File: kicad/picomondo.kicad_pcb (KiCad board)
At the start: 4 copper layers, 120 x 90 mm, 289 parts, among them J1 EdgeLock J1, J10 SWD, J11 Barrel 5.5x2.1, J12 Terminal 2P, J13 USB-C, J14 Arduino power, J15 Arduino analog, J16 Arduino digital 0-7, J17 Arduino digital 8-13, J18 Pico left (pins 1-20), J19 Pico right (pins 40-21), J2 EdgeLock J2, J3 EdgeLock J3, J4 EdgeLock J4, J5 EdgeLock J5, J6 EdgeLock J6, J7 J7 5V out, J8 J8 V_INPUT out, J9 EdgeLock J9, Q1 CSD18543Q3A, Q2 CSD18543Q3A, Q3 SI2305A, Q4 MMBT3904, Q5 DMP4015SSS-13, Q6 MMBT3904, Q7 SI2305A, Q8 MMBT3904, SW1 BOOTSEL, SW2 RESET, U1 RP2350B, U10 STUSB4500, U11 microSD, U2 W25Q128JVS, U3 DNP second memory, U4 TPS55288, U5 AP2112K-3.3, U6 AP2112K-3.3, U7 INA226 (0x40), U8 INA226 (0x41), U9 USBLC6-2SC6, Y1 ABM8-272-T3

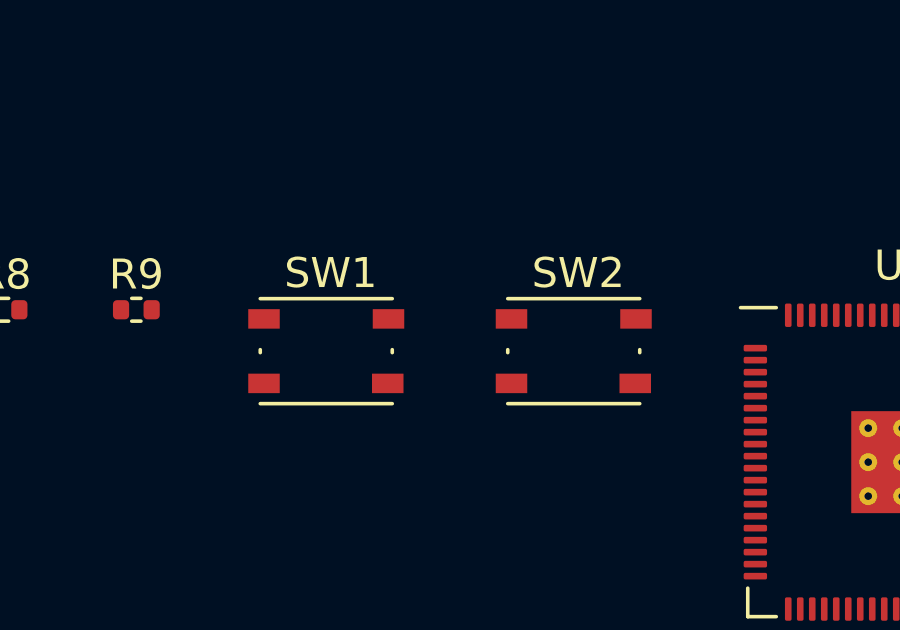
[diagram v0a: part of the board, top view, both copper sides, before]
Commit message: Pick JLCPCB parts for the whole BOM and add BOM/CPL generation
Adds bom/parts.csv (LCSC numbers and MPNs), scripts to apply it to the schematic and
board and to generate the JLCPCB BOM, CPL and a live stock report. Swaps the
BOOTSEL/RESET switch to a basic 5.1 mm part with a matching footprint, and replaces
out-of-stock parts (SS54, WS2812B, 10u caps, SWD header).

Co-Authored-By: Claude Sonnet 5.5 <noreply@anthropic.com>
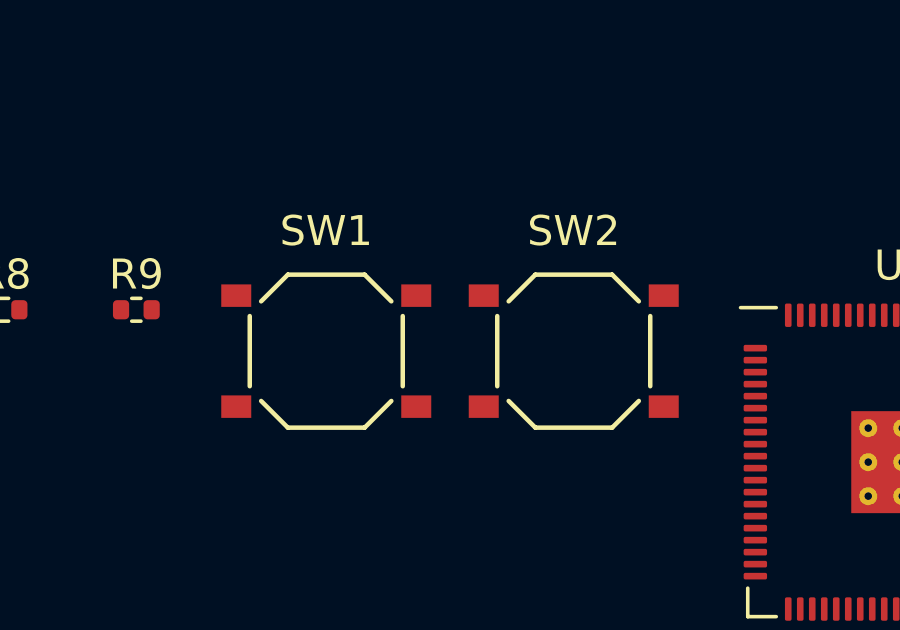
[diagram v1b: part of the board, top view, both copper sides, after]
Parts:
- SW1, SW2: footprint Button_Switch_SMD:SW_Push_1P1T_NO_Vertical_Wuerth_434133025816 -> picomondo:SW_SMD_TS-1187A_5.1x5.1

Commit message: Rework board layout, swap SWD header to through-hole, add Qwiic port
- SWD (J10) is now a 1x3 2.54 mm through-hole pin header footprint
  (SWCLK, GND, SWDIO) instead of the JST SH connector; removed from the
  JLCPCB BOM.
- Add J20 Qwiic connector (XY-SM04B-SRSS-TB) on the I2C bus: GND, +3V3,
  GPIO20 (SDA), GPIO21 (SCL), mounting tabs to GND.
- Placement/routing progress and the helper scripts used for it.

DRC still reports open items (unrouted RUN/GPIO24/GPIO29/QSPI_SD0 nets,
R108/GPIO23 and NT1/GPIO20 shorts, J12 edge clearance, silkscreen
overlaps); to be fixed in follow-up commits.

Co-Authored-By: Claude Sonnet 5.5 <noreply@anthropic.com>
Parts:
- removed JP1, JP2, JP3, JP4, JP5, JP6, JP7, JP8: LED enable, Jumper:SolderJumper-2_P1.3mm_Open_RoundedPad1.0x1.5mm
- added CN1: QWICC, JLCImport:XY-SM04B-SRSS-TB, F.Cu at (146.3, 80.1)
- J10: footprint Connector_JST:JST_SH_SM03B-SRSS-TB_1x03-1MP_P1.00mm_Horizontal -> Connector_PinHeader_2.54mm:PinHeader_1x03_P2.54mm_Horizontal
- TP1, TP10, TP11, TP12, TP13, TP14, TP15, TP16, TP17, TP2, TP3, TP4, TP5, TP6, TP7, TP8, TP9: moved to B.Cu
- moved R95 446.6 mm to (41.1, 43.0), turned to -90 degrees
- moved R97 429.0 mm to (67.7, 43.0), turned to -90 degrees
- moved R94 427.1 mm to (56.4, 43.0), turned to -90 degrees
- moved R99 411.5 mm to (94.3, 43.0), turned to -90 degrees
- moved R96 409.7 mm to (83.0, 43.0), turned to -90 degrees
- moved R89 409.0 mm to (46.0, 107.0), turned to 90 degrees
- moved R88 406.5 mm to (44.0, 107.0), turned to 90 degrees
- moved R91 406.5 mm to (57.3, 107.0), turned to 90 degrees
- moved R90 404.1 mm to (55.3, 107.0), turned to 90 degrees
- moved R98 392.2 mm to (109.6, 43.0), turned to -90 degrees
- moved R93 384.9 mm to (87.9, 103.2), turned to 90 degrees
- moved R92 378.0 mm to (90.4, 103.1), turned to 90 degrees
- moved R86 369.1 mm to (72.6, 107.0), turned to 90 degrees
- moved R87 364.3 mm to (81.9, 107.0), turned to 90 degrees
- moved R73 349.4 mm to (43.1, 43.0), turned to -90 degrees
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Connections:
- R100 pad 1: /GPIO indicators/LED46_J -> GPIO46
- R101 pad 1: /GPIO indicators/LED47_J -> GPIO47
- R108 pad 2: GPIO23 -> unconnected-(R108-Pad2)
- R94 pad 1: /GPIO indicators/LED40_J -> GPIO40
- R95 pad 1: /GPIO indicators/LED41_J -> GPIO41
- R96 pad 1: /GPIO indicators/LED42_J -> GPIO42
- R97 pad 1: /GPIO indicators/LED43_J -> GPIO43
- R98 pad 1: /GPIO indicators/LED44_J -> GPIO44
- R99 pad 1: /GPIO indicators/LED45_J -> GPIO45
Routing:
- net +3V3: track 0.00 -> 471.4 mm, vias 0 -> 72
- net GND: track 0.00 -> 377.3 mm, vias 0 -> 110
- net +5V: track 0.00 -> 291.2 mm, vias 0 -> 21
- net GPIO20: track 0.00 -> 240.9 mm, vias 0 -> 24
- net V_INPUT: track 0.00 -> 230.0 mm, vias 0 -> 23
- net GPIO21: track 0.00 -> 221.7 mm, vias 0 -> 20
- net +3V3_AUX: track 0.00 -> 145.1 mm, vias 0 -> 9
- net VBUS: track 0.00 -> 128.5 mm, vias 0 -> 14
- net +1V1: track 0.00 -> 127.5 mm, vias 0 -> 16
- net USB_D+: track 0.00 -> 127.3 mm, vias 0 -> 8
- net +5V_SW: track 0.00 -> 123.5 mm, vias 0 -> 9
- net GPIO28: track 0.00 -> 119.4 mm, vias 0 -> 8
- net GPIO1: track 0.00 -> 119.3 mm, vias 0 -> 7
- net GPIO18: track 0.00 -> 118.3 mm, vias 0 -> 5
- net GPIO0: track 0.00 -> 117.9 mm, vias 0 -> 10
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- added copper zone on B.Cu, net GND
- removed copper zone on In1.Cu, net GND
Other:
- board text removed: "3V3 REGULATORS"
- board text removed: "5V BUCK-BOOST"
- board text removed: "ARDUINO AND PICO HEADERS"
- board text removed: "BOARD SUPPORT"
- board text removed: "EDGELOCK CONNECTORS"
- board text removed: "GPIO INDICATORS"
- board text removed: "MCU CORE"
- board text removed: "POWER INPUT"
- board text removed: "Pico outline (not fabricated)"
- board text removed: "SWITCHED OUTPUTS"
- board text removed: "USB-C PD"
